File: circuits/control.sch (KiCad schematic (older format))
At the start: 6 parts, among them Q1 Q_MBT3904, Q2 Q_IRF7907TRPBF

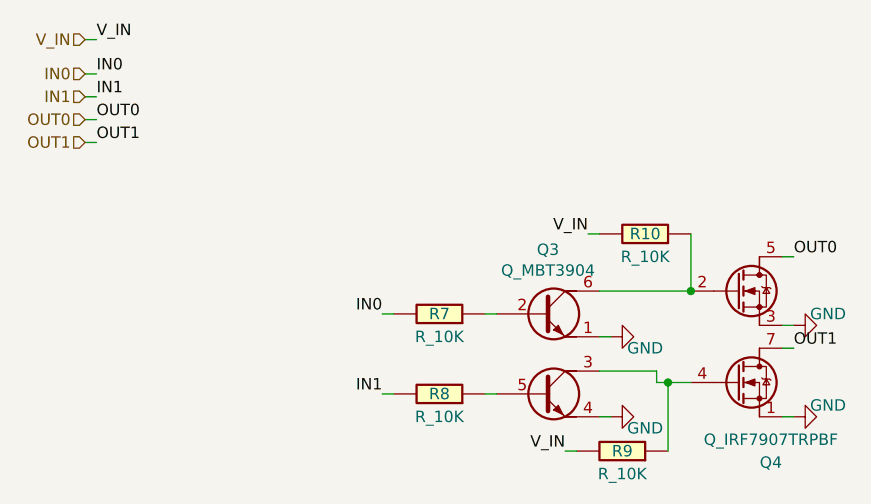
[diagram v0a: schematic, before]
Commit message: finished schematic corrections, working on layout
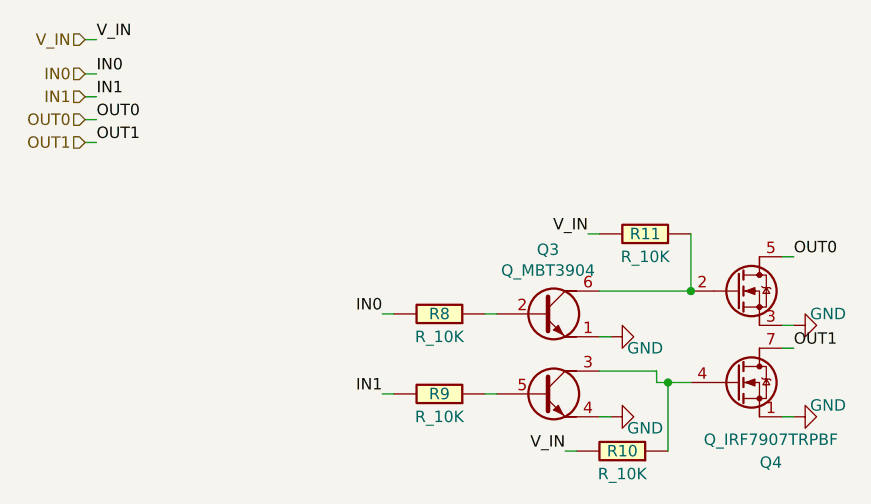
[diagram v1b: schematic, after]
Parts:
- renumbered R3 to R4, R4 to R5, R5 to R6, R6 to R7
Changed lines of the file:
@@
 AR Path="/5FE8FE83/600435CF" Ref="R?"  Part="1"
 AR Path="/5FE5EA71/600435CF" Ref="R?"  Part="1"
-AR Path="/60030996/600435CF" Ref="R5"  Part="1"
+AR Path="/60030996/600435CF" Ref="R6"  Part="1"
 AR Path="/600E925B/600F0FE9/600435CF" Ref="R?"  Part="1"
 AR Path="/600F4C7B/600435CF" Ref="R?"  Part="1"
-AR Path="/605FA739/600435CF" Ref="R9"  Part="1"
-F 0 "R9" V 3500 2850 50  0000 C CNN
+AR Path="/605FA739/600435CF" Ref="R10"  Part="1"
+F 0 "R10" V 3500 2850 50  0000 C CNN
 F 1 "R_10K" V 3400 2850 50  0000 C CNN
 F 2 "Resistor_SMD:R_0603_1608Metric_Pad0.98x0.95mm_HandSolder" V 3430 2850 50  0001 C CNN
@@
 AR Path="/5FE8FE83/600435D9" Ref="R?"  Part="1"
 AR Path="/5FE5EA71/600435D9" Ref="R?"  Part="1"
-AR Path="/60030996/600435D9" Ref="R4"  Part="1"
+AR Path="/60030996/600435D9" Ref="R5"  Part="1"
 AR Path="/600E925B/600F0FE9/600435D9" Ref="R?"  Part="1"
 AR Path="/600F4C7B/600435D9" Ref="R?"  Part="1"
-AR Path="/605FA739/600435D9" Ref="R8"  Part="1"
-F 0 "R8" V 2700 2600 50  0000 C CNN
+AR Path="/605FA739/600435D9" Ref="R9"  Part="1"
+F 0 "R9" V 2700 2600 50  0000 C CNN
 F 1 "R_10K" V 2600 2600 50  0000 C CNN
 F 2 "Resistor_SMD:R_0603_1608Metric_Pad0.98x0.95mm_HandSolder" V 2630 2600 50  0001 C CNN
@@
 AR Path="/5FE8FE83/600435E2" Ref="R?"  Part="1"
 AR Path="/5FE5EA71/600435E2" Ref="R?"  Part="1"
-AR Path="/60030996/600435E2" Ref="R3"  Part="1"
+AR Path="/60030996/600435E2" Ref="R4"  Part="1"
 AR Path="/600E925B/600F0FE9/600435E2" Ref="R?"  Part="1"
 AR Path="/600F4C7B/600435E2" Ref="R?"  Part="1"
-AR Path="/605FA739/600435E2" Ref="R7"  Part="1"
-F 0 "R7" V 2700 2250 50  0000 C CNN
+AR Path="/605FA739/600435E2" Ref="R8"  Part="1"
+F 0 "R8" V 2700 2250 50  0000 C CNN
 F 1 "R_10K" V 2600 2250 50  0000 C CNN
 F 2 "Resistor_SMD:R_0603_1608Metric_Pad0.98x0.95mm_HandSolder" V 2630 2250 50  0001 C CNN
@@
 AR Path="/5FE8FE83/6004360A" Ref="R?"  Part="1"
 AR Path="/5FE5EA71/6004360A" Ref="R?"  Part="1"
-AR Path="/60030996/6004360A" Ref="R6"  Part="1"
+AR Path="/60030996/6004360A" Ref="R7"  Part="1"
 AR Path="/600E925B/600F0FE9/6004360A" Ref="R?"  Part="1"
 AR Path="/600F4C7B/6004360A" Ref="R?"  Part="1"
-AR Path="/605FA739/6004360A" Ref="R10"  Part="1"
-F 0 "R10" V 3600 1900 50  0000 C CNN
+AR Path="/605FA739/6004360A" Ref="R11"  Part="1"
+F 0 "R11" V 3600 1900 50  0000 C CNN
 F 1 "R_10K" V 3500 1900 50  0000 C CNN
 F 2 "Resistor_SMD:R_0603_1608Metric_Pad0.98x0.95mm_HandSolder" V 3530 1900 50  0001 C CNN
@@
 AR Path="/5FDE4427" Ref="#PWR?"  Part="1"
 AR Path="/5A7BADB8/5FDE4427" Ref="#PWR?"  Part="1"
-AR Path="/60030996/5FDE4427" Ref="#PWR024"  Part="1"
-AR Path="/605FA739/5FDE4427" Ref="#PWR028"  Part="1"
-F 0 "#PWR028" H 4250 2050 50  0001 C CNN
+AR Path="/60030996/5FDE4427" Ref="#PWR023"  Part="1"
+AR Path="/605FA739/5FDE4427" Ref="#PWR027"  Part="1"
+F 0 "#PWR027" H 4250 2050 50  0001 C CNN
 F 1 "GND" V 4300 2150 50  0000 C CNN
 F 2 "" H 4250 2300 50  0001 C CNN
@@
 AR Path="/5FDE59F9" Ref="#PWR?"  Part="1"
 AR Path="/5A7BADB8/5FDE59F9" Ref="#PWR?"  Part="1"
-AR Path="/60030996/5FDE59F9" Ref="#PWR025"  Part="1"
-AR Path="/605FA739/5FDE59F9" Ref="#PWR029"  Part="1"
-F 0 "#PWR029" H 4250 2450 50  0001 C CNN
+AR Path="/60030996/5FDE59F9" Ref="#PWR024"  Part="1"
+AR Path="/605FA739/5FDE59F9" Ref="#PWR028"  Part="1"
+F 0 "#PWR028" H 4250 2450 50  0001 C CNN
 F 1 "GND" V 4300 2550 50  0000 C CNN
 F 2 "" H 4250 2700 50  0001 C CNN
@@
 AR Path="/5FDE8400" Ref="#PWR?"  Part="1"
 AR Path="/5A7BADB8/5FDE8400" Ref="#PWR?"  Part="1"
-AR Path="/60030996/5FDE8400" Ref="#PWR023"  Part="1"
-AR Path="/605FA739/5FDE8400" Ref="#PWR027"  Part="1"
-F 0 "#PWR027" H 3450 2450 50  0001 C CNN
+AR Path="/60030996/5FDE8400" Ref="#PWR022"  Part="1"
+AR Path="/605FA739/5FDE8400" Ref="#PWR026"  Part="1"
+F 0 "#PWR026" H 3450 2450 50  0001 C CNN
 F 1 "GND" V 3400 2550 50  0000 C CNN
 F 2 "" H 3450 2700 50  0001 C CNN
@@
 AR Path="/5FDEC0EE" Ref="#PWR?"  Part="1"
 AR Path="/5A7BADB8/5FDEC0EE" Ref="#PWR?"  Part="1"
-AR Path="/60030996/5FDEC0EE" Ref="#PWR022"  Part="1"
-AR Path="/605FA739/5FDEC0EE" Ref="#PWR026"  Part="1"
-F 0 "#PWR026" H 3450 2100 50  0001 C CNN
+AR Path="/60030996/5FDEC0EE" Ref="#PWR021"  Part="1"
+AR Path="/605FA739/5FDEC0EE" Ref="#PWR025"  Part="1"
+F 0 "#PWR025" H 3450 2100 50  0001 C CNN
 F 1 "GND" V 3400 2200 50  0000 C CNN
 F 2 "" H 3450 2350 50  0001 C CNN
